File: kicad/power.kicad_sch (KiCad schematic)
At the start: 29 parts, among them U1 RT9471GQW, U2 MCP1663T-E/MNY, U3 MCP1603-330I/MC

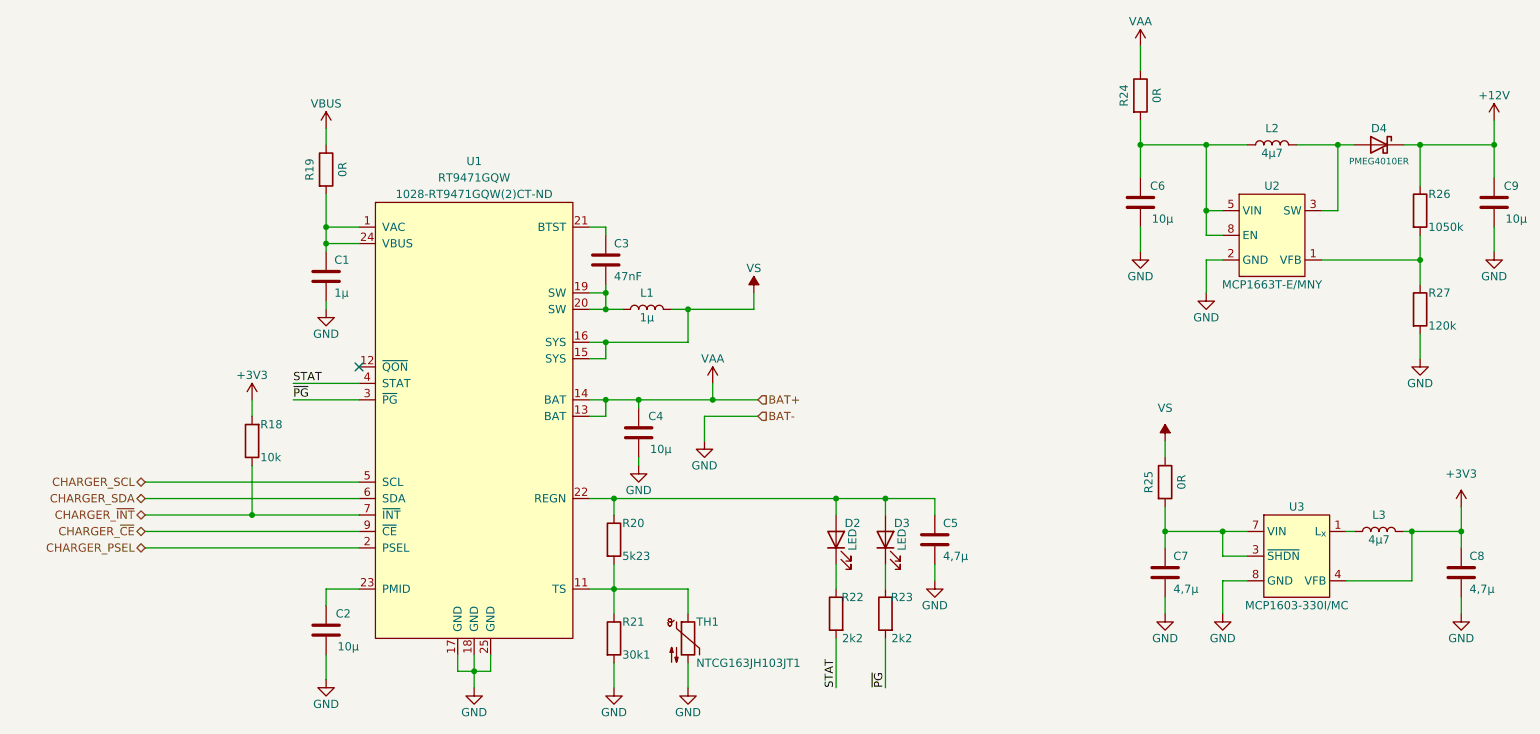
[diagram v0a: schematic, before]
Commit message: remove Rx with 0 Ohms
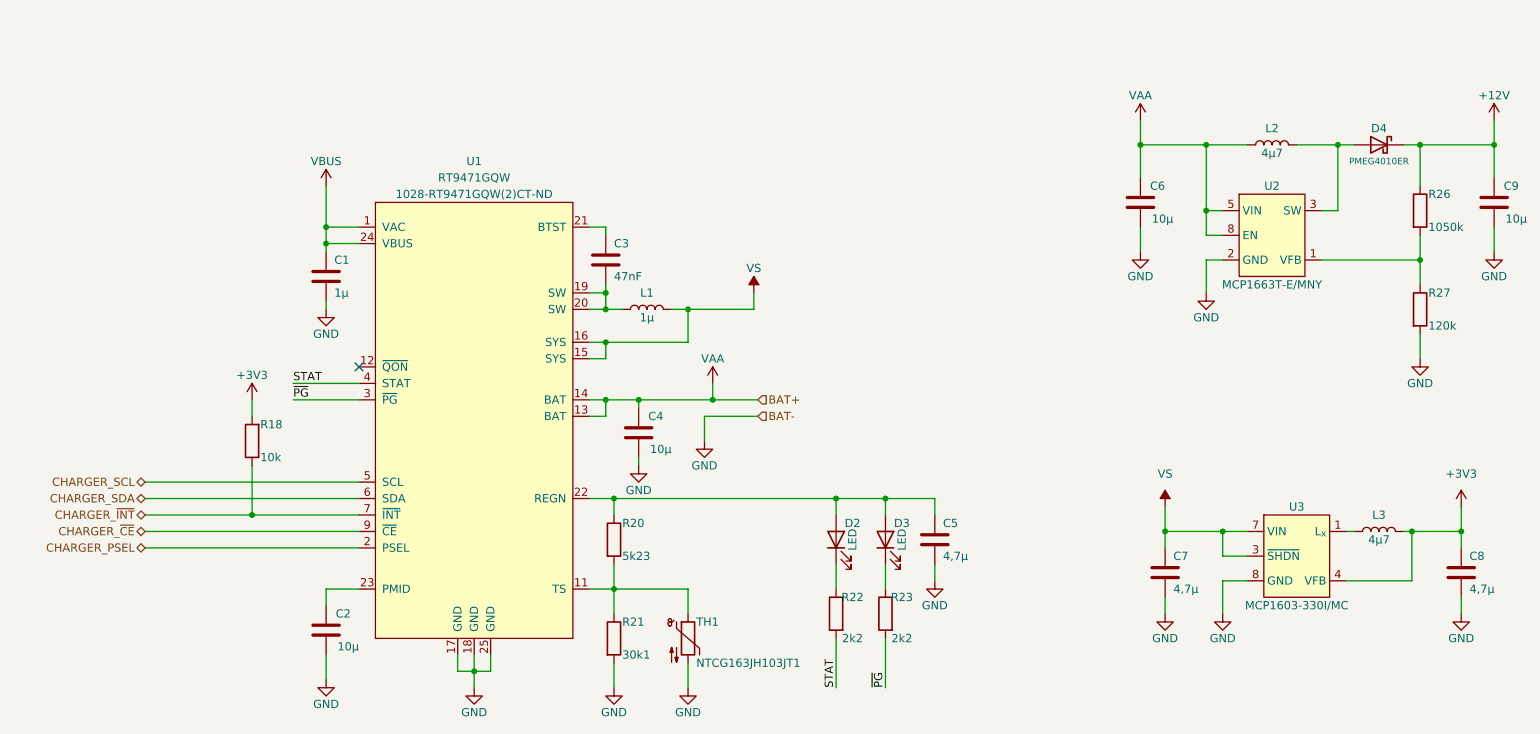
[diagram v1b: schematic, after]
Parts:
- removed R19, R24, R25: 0R, Resistor_SMD:R_0603_1608Metric, symbol Device:R
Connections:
- net VAA: now also C6.1, L2.1, U2.5 (VIN), U2.8 (EN)
- net VBUS: now also C1.1, U1.1 (VAC), U1.24 (VBUS)
- net VS: now also C7.1, U3.3 (~{SHDN}), U3.7 (VIN)
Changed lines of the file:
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@@
+    (stroke (width 0) (type default) (color 0 0 0 0))
+  )
+  (wire (pts (xy 204.47 107.95) (xy 204.47 111.76))
+    (stroke (width 0) (type default) (color 0 0 0 0))
+  )
+  (wire (pts (xy 95.25 133.35) (xy 97.79 133.35))
+    (stroke (width 0) (type default) (color 0 0 0 0))
+  )
+  (wire (pts (xy 119.38 135.89) (xy 119.38 132.08))
+    (stroke (width 0) (type default) (color 0 0 0 0))
+  )
+  (wire (pts (xy 242.57 111.76) (xy 242.57 119.38))
+    (stroke (width 0) (type default) (color 0 0 0 0))
+  )
+  (wire (pts (xy 204.47 111.76) (xy 213.36 111.76))
+    (stroke (width 0) (type default) (color 0 0 0 0))
+  )
+  (wire (pts (xy 46.99 111.76) (xy 80.01 111.76))
+    (stroke (width 0) (type default) (color 0 0 0 0))
+  )
+  (wire (pts (xy 217.17 119.38) (xy 213.36 119.38))
+    (stroke (width 0) (type default) (color 0 0 0 0))
+  )
+  (wire (pts (xy 130.81 120.65) (xy 130.81 124.46))
+    (stroke (width 0) (type default) (color 0 0 0 0))
+  )
+  (wire (pts (xy 213.36 69.85) (xy 210.82 69.85))
+    (stroke (width 0) (type default) (color 0 0 0 0))
+  )
+  (wire (pts (xy 63.5 109.22) (xy 80.01 109.22))
+    (stroke (width 0) (type default) (color 0 0 0 0))
+  )
+  (wire (pts (xy 46.99 109.22) (xy 63.5 109.22))
+    (stroke (width 0) (type default) (color 0 0 0 0))
+  )
+  (wire (pts (xy 161.29 106.68) (xy 168.91 106.68))
+    (stroke (width 0) (type default) (color 0 0 0 0))
+  )
+  (wire (pts (xy 115.57 85.09) (xy 118.11 85.09))
+    (stroke (width 0) (type default) (color 0 0 0 0))
+  )
+  (wire (pts (xy 100.33 133.35) (xy 97.79 133.35))
+    (stroke (width 0) (type default) (color 0 0 0 0))
+  )
+  (wire (pts (xy 232.41 111.76) (xy 233.68 111.76))
     (stroke (width 0) (type default) (color 0 0 0 0))
   )
@@
     (stroke (width 0) (type default) (color 0 0 0 0))
   )
-  (wire (pts (xy 74.93 59.69) (xy 74.93 64.77))
-    (stroke (width 0) (type default) (color 0 0 0 0))
-  )
-  (wire (pts (xy 204.47 97.79) (xy 204.47 100.33))
-    (stroke (width 0) (type default) (color 0 0 0 0))
-  )
-  (wire (pts (xy 95.25 133.35) (xy 97.79 133.35))
-    (stroke (width 0) (type default) (color 0 0 0 0))
-  )
-  (wire (pts (xy 119.38 135.89) (xy 119.38 132.08))
-    (stroke (width 0) (type default) (color 0 0 0 0))
-  )
-  (wire (pts (xy 242.57 111.76) (xy 242.57 119.38))
-    (stroke (width 0) (type default) (color 0 0 0 0))
-  )
-  (wire (pts (xy 204.47 111.76) (xy 213.36 111.76))
-    (stroke (width 0) (type default) (color 0 0 0 0))
-  )
-  (wire (pts (xy 46.99 111.76) (xy 80.01 111.76))
-    (stroke (width 0) (type default) (color 0 0 0 0))
-  )
-  (wire (pts (xy 217.17 119.38) (xy 213.36 119.38))
-    (stroke (width 0) (type default) (color 0 0 0 0))
-  )
-  (wire (pts (xy 130.81 120.65) (xy 130.81 124.46))
-    (stroke (width 0) (type default) (color 0 0 0 0))
-  )
-  (wire (pts (xy 213.36 69.85) (xy 210.82 69.85))
-    (stroke (width 0) (type default) (color 0 0 0 0))
-  )
-  (wire (pts (xy 63.5 109.22) (xy 80.01 109.22))
-    (stroke (width 0) (type default) (color 0 0 0 0))
-  )
-  (wire (pts (xy 46.99 109.22) (xy 63.5 109.22))
-    (stroke (width 0) (type default) (color 0 0 0 0))
-  )
-  (wire (pts (xy 161.29 106.68) (xy 168.91 106.68))
-    (stroke (width 0) (type default) (color 0 0 0 0))
-  )
-  (wire (pts (xy 115.57 85.09) (xy 118.11 85.09))
-    (stroke (width 0) (type default) (color 0 0 0 0))
-  )
-  (wire (pts (xy 100.33 133.35) (xy 97.79 133.35))
-    (stroke (width 0) (type default) (color 0 0 0 0))
-  )
-  (wire (pts (xy 232.41 111.76) (xy 233.68 111.76))
-    (stroke (width 0) (type default) (color 0 0 0 0))
-  )
-  (wire (pts (xy 200.66 36.83) (xy 200.66 40.64))
-    (stroke (width 0) (type default) (color 0 0 0 0))
-  )
   (wire (pts (xy 243.84 81.28) (xy 243.84 85.09))
     (stroke (width 0) (type default) (color 0 0 0 0))
@@
     (stroke (width 0) (type default) (color 0 0 0 0))
   )
-  (wire (pts (xy 74.93 49.53) (xy 74.93 52.07))
+  (wire (pts (xy 74.93 58.42) (xy 74.93 64.77))
     (stroke (width 0) (type default) (color 0 0 0 0))
   )
@@
   )
   (wire (pts (xy 123.19 100.33) (xy 123.19 101.6))
-    (stroke (width 0) (type default) (color 0 0 0 0))
-  )
-  (wire (pts (xy 204.47 107.95) (xy 204.47 111.76))
     (stroke (width 0) (type default) (color 0 0 0 0))
   )
@@
     (pin "2")
   )
-  (symbol (lib_id "power:VS") (at 204.47 97.79 0) (unit 1)
+  (symbol (lib_id "power:VS") (at 204.47 107.95 0) (unit 1)
     (in_bom yes) (on_board yes) (fields_autoplaced)
-    (property "Reference" "#PWR038" (id 0) (at 199.39 101.6 0)
-      (effects (font (size 1.27 1.27)) hide)
-    )
-    (property "Value" "VS" (id 1) (at 204.47 92.71 0))
-    (property "Footprint" "" (id 2) (at 204.47 97.79 0)
-      (effects (font (size 1.27 1.27)) hide)
-    )
-    (property "Datasheet" "" (id 3) (at 204.47 97.79 0)
+    (property "Reference" "#PWR038" (id 0) (at 199.39 111.76 0)
+      (effects (font (size 1.27 1.27)) hide)
+    )
+    (property "Value" "VS" (id 1) (at 204.47 102.87 0))
+    (property "Footprint" "" (id 2) (at 204.47 107.95 0)
+      (effects (font (size 1.27 1.27)) hide)
+    )
+    (property "Datasheet" "" (id 3) (at 204.47 107.95 0)
       (effects (font (size 1.27 1.27)) hide)
     )
@@
     (pin "1")
   )
-  (symbol (lib_id "power:VBUS") (at 74.93 49.53 0) (unit 1)
-    (in_bom yes) (on_board yes)
-    (property "Reference" "#PWR025" (id 0) (at 74.93 53.34 0)
-      (effects (font (size 1.27 1.27)) hide)
-    )
-    (property "Value" "VBUS" (id 1) (at 74.93 45.72 0))
-    (property "Footprint" "" (id 2) (at 74.93 49.53 0)
-      (effects (font (size 1.27 1.27)) hide)
-    )
-    (property "Datasheet" "" (id 3) (at 74.93 49.53 0)
+  (symbol (lib_id "power:VBUS") (at 74.93 58.42 0) (unit 1)
+    (in_bom yes) (on_board yes)
+    (property "Reference" "#PWR025" (id 0) (at 74.93 62.23 0)
+      (effects (font (size 1.27 1.27)) hide)
+    )
+    (property "Value" "VBUS" (id 1) (at 74.93 54.61 0))
+    (property "Footprint" "" (id 2) (at 74.93 58.42 0)
+      (effects (font (size 1.27 1.27)) hide)
+    )
+    (property "Datasheet" "" (id 3) (at 74.93 58.42 0)
       (effects (font (size 1.27 1.27)) hide)
     )
@@
     (pin "1")
   )
-  (symbol (lib_id "Device:R") (at 200.66 44.45 0) (unit 1)
-    (in_bom yes) (on_board yes)
-    (property "Reference" "R24" (id 0) (at 198.12 44.45 90))
-    (property "Value" "0R" (id 1) (at 203.2 44.45 90))
-    (property "Footprint" "Resistor_SMD:R_0603_1608Metric" (id 2) (at 198.882 44.45 90)
-      (effects (font (size 1.27 1.27)) hide)
-    )
-    (property "Datasheet" "~" (id 3) (at 200.66 44.45 0)
-      (effects (font (size 1.27 1.27)) hide)
-    )
-    (property "Digikey" "541-0.0SBCT-ND" (id 4) (at 200.66 44.45 0)
-      (effects (font (size 1.27 1.27)) hide)
-    )
-    (pin "1")
-    (pin "2")
-  )
   (symbol (lib_id "power:GND") (at 250.19 124.46 0) (unit 1)
     (in_bom yes) (on_board yes)
@@
     (pin "1")
   )
-  (symbol (lib_id "power:VAA") (at 200.66 36.83 0) (unit 1)
-    (in_bom yes) (on_board yes)
-    (property "Reference" "#PWR036" (id 0) (at 200.66 40.64 0)
-      (effects (font (size 1.27 1.27)) hide)
-    )
-    (property "Value" "VAA" (id 1) (at 200.66 33.02 0))
-    (property "Footprint" "" (id 2) (at 200.66 36.83 0)
-      (effects (font (size 1.27 1.27)) hide)
-    )
-    (property "Datasheet" "" (id 3) (at 200.66 36.83 0)
+  (symbol (lib_id "power:VAA") (at 200.66 48.26 0) (unit 1)
+    (in_bom yes) (on_board yes)
+    (property "Reference" "#PWR036" (id 0) (at 200.66 52.07 0)
+      (effects (font (size 1.27 1.27)) hide)
+    )
+    (property "Value" "VAA" (id 1) (at 200.66 44.45 0))
+    (property "Footprint" "" (id 2) (at 200.66 48.26 0)
+      (effects (font (size 1.27 1.27)) hide)
+    )
+    (property "Datasheet" "" (id 3) (at 200.66 48.26 0)
       (effects (font (size 1.27 1.27)) hide)
     )
@@
     (pin "9")
   )
-  (symbol (lib_id "Device:R") (at 74.93 55.88 0) (unit 1)
-    (in_bom yes) (on_board yes)
-    (property "Reference" "R19" (id 0) (at 72.39 55.88 90))
-    (property "Value" "0R" (id 1) (at 77.47 55.88 90))
-    (property "Footprint" "Resistor_SMD:R_0603_1608Metric" (id 2) (at 73.152 55.88 90)
-      (effects (font (size 1.27 1.27)) hide)
-    )
-    (property "Datasheet" "~" (id 3) (at 74.93 55.88 0)
-      (effects (font (size 1.27 1.27)) hide)
-    )
-    (property "Digikey" "541-0.0SBCT-ND" (id 4) (at 74.93 55.88 0)
-      (effects (font (size 1.27 1.27)) hide)
-    )
-    (pin "1")
-    (pin "2")
-  )
-  (symbol (lib_id "Device:R") (at 204.47 104.14 0) (unit 1)
-    (in_bom yes) (on_board yes)
-    (property "Reference" "R25" (id 0) (at 201.93 104.14 90))
-    (property "Value" "0R" (id 1) (at 207.01 104.14 90))
-    (property "Footprint" "Resistor_SMD:R_0603_1608Metric" (id 2) (at 202.692 104.14 90)
-      (effects (font (size 1.27 1.27)) hide)
-    )
-    (property "Datasheet" "~" (id 3) (at 204.47 104.14 0)
-      (effects (font (size 1.27 1.27)) hide)
-    )
-    (property "Digikey" "541-0.0SBCT-ND" (id 4) (at 204.47 104.14 0)
-      (effects (font (size 1.27 1.27)) hide)
-    )
-    (pin "1")
-    (pin "2")
-  )
   (symbol (lib_id "Device:C") (at 200.66 60.96 0) (mirror y) (unit 1)
